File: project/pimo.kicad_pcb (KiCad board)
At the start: 2 copper layers, 65 x 56.5 mm, 11 parts, among them J1 RPi_GPIO, J11 Conn_01x03_Pin, J2 Conn_01x05_Pin, J3 Conn_ARM_JTAG_SWD_10, J4 Conn_01x01, U1 W25Q32JVSS

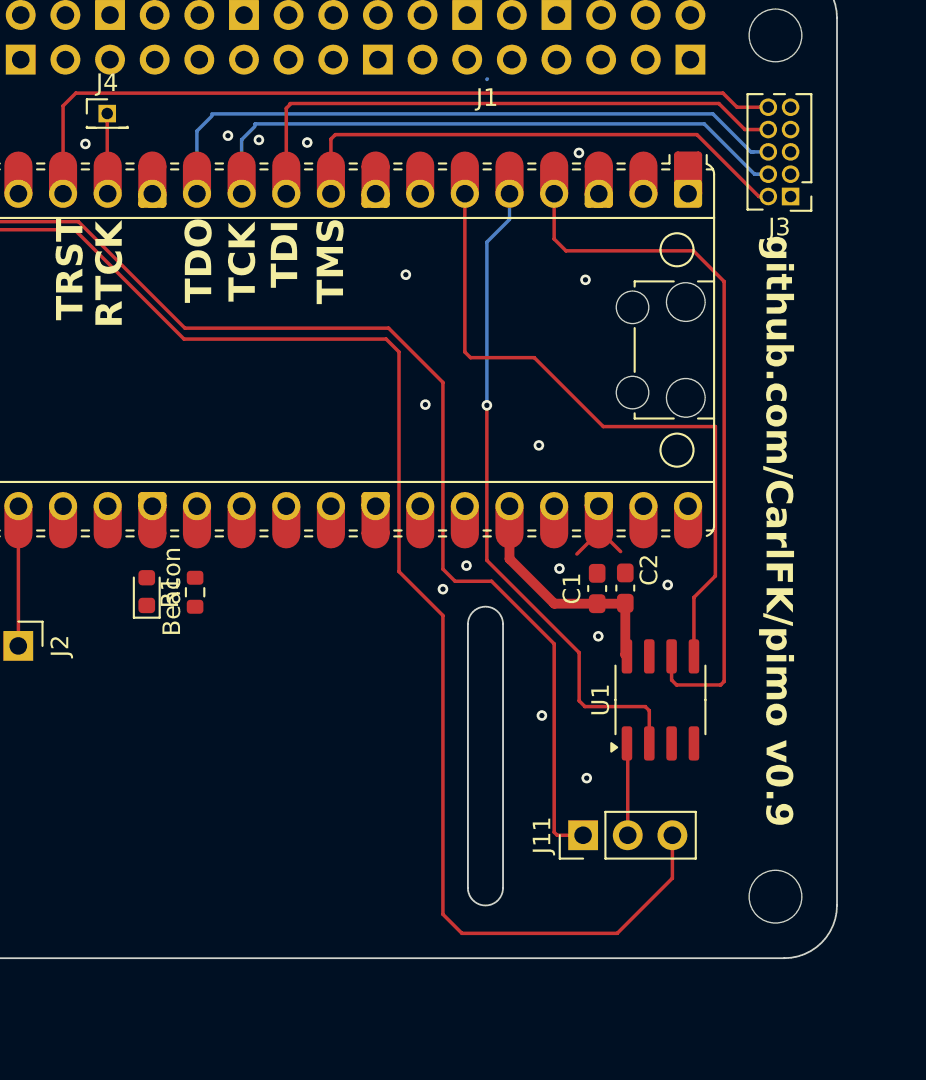
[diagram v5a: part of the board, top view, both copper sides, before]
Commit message: bonus jtag header
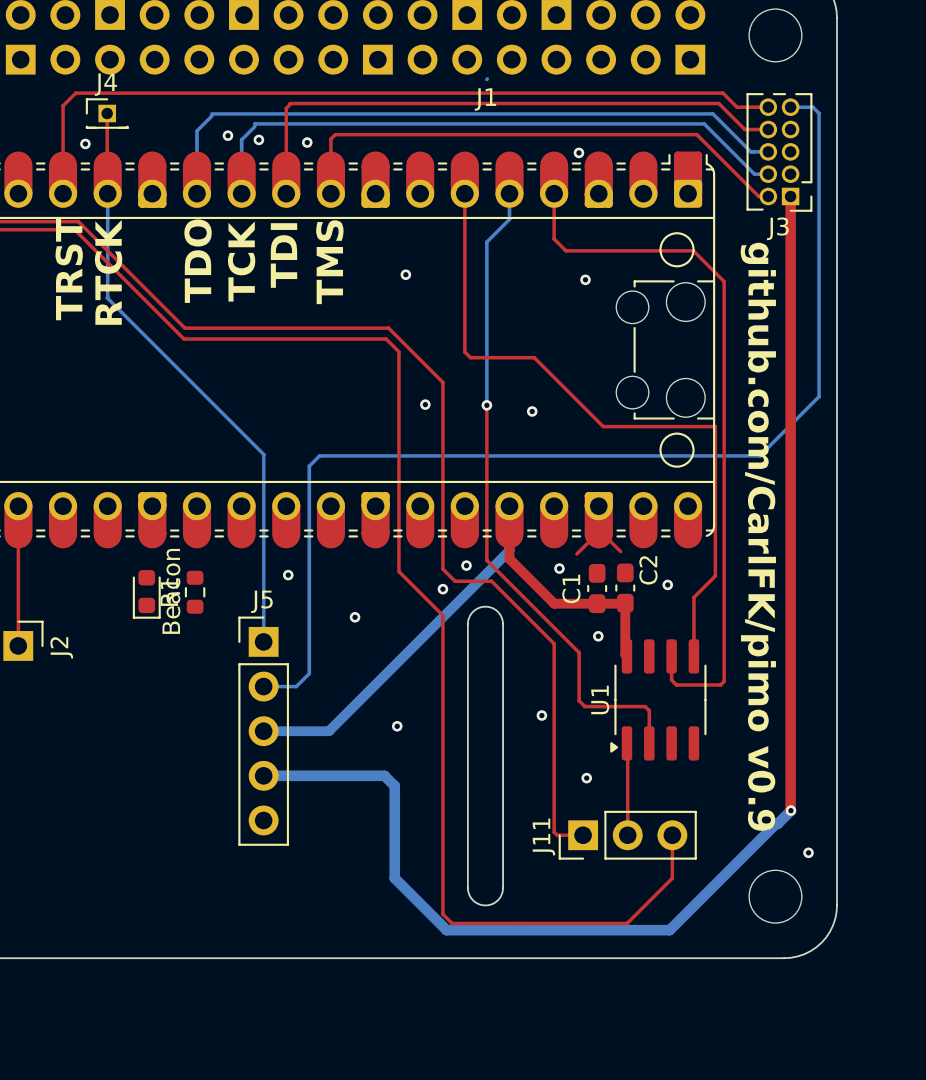
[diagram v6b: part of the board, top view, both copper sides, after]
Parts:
- added J5: Conn_01x05_Pin, Connector_PinHeader_2.54mm:PinHeader_1x05_P2.54mm_Vertical, F.Cu at (68.8, 79.0)
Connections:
- net /pico3v3 renamed /3V3
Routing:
- net /VTref: track 0.00 -> 74.5 mm, vias 0 -> 1
- net /GNDDetect: track 0.00 -> 63.2 mm
- net /RTCK: track 4.57 -> 33.8 mm
- net /3V3: track 13.7 -> 34.5 mm
- net GND: vias 24 -> 28

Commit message: label v1.0
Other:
- board text added: "github.com/CarlFK/pimo v1.0"
- board text removed: "github.com/CarlFK/pimo v0.9"
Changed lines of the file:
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@@
 		)
 	)
-	(gr_text "github.com/CarlFK/pimo v0.9"
+	(gr_text "github.com/CarlFK/pimo v1.0"
 		(at 96.2 56.2 270)
 		(layer "F.SilkS")

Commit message: pmod header.  v1.1
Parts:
- added J6: 2.54-2*6P Bend insert, TinyTapeout_PMOD:PinHeader_2x06_P2.54mm_PMODPeriph2B, F.Cu at (96.1, 75.8)
- added R2: 1k, Resistor_SMD:R_0603_1608Metric, F.Cu at (87.8, 86.8)
- added REF**: OSHW-Logo_5.7x6mm_SilkScreen, Symbol:OSHW-Logo_5.7x6mm_SilkScreen, F.Cu at (63.2, 85.0)
- added REF**: KiCad-Logo2_5mm_SilkScreen, Symbol:KiCad-Logo2_5mm_SilkScreen, F.Cu at (50.9, 84.4)
- moved D1 0.16 mm to (62.0, 76.2), turned to -90 degrees
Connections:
- net /3V3 renamed +3.3V
- net /RPI_SPI_CLK renamed PMOD4
- net /RPI_SPI_MISO renamed PMOD3
- net /RPI_SPI_MOSI renamed PMOD2
- net Net-(J11-Pin_2) renamed PMOD1_IN
- A1 pad 29: GND -> Net-(A1-GPIO22)
- D1 pad 2: GND -> Net-(D1-A)
- R1 pad 1: GND -> Net-(D1-A)
- R1 pad 2: GND -> Net-(A1-GPIO22)
- U1 pad 3: unconnected-(U1-IO2-Pad3) -> PMOD5
- U1 pad 7: unconnected-(U1-IO3-Pad7) -> PMOD6
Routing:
- net +3.3V: track 34.5 -> 58.7 mm, vias 0 -> 2
- net PMOD6: track 0.00 -> 12.7 mm
- net PMOD5: track 0.00 -> 8.98 mm
- net PMOD1_IN: track 5.24 -> 14.0 mm
- net PMOD2: track 38.6 -> 46.7 mm, vias 0 -> 1
- net PMOD3: track 37.6 -> 43.1 mm
- net /VTref: track 74.5 -> 78.6 mm, vias 1 -> 0
- net Net-(A1-GPIO22): track 0.00 -> 4.11 mm
- net Net-(D1-A): track 0.00 -> 2.78 mm
- net PMOD4: track 40.5 -> 42.7 mm
- net GND: track 3.56 -> 3.88 mm, vias 28 -> 29
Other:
- board text added: "github.com/CarlFK/pimo v1.1"
- board text removed: "github.com/CarlFK/pimo v1.0"
